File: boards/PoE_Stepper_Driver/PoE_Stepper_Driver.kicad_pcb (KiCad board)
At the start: 2 copper layers, 97.8 x 71.1 mm, 135 parts, among them J1 RJ45, J2 Motor, J3 Limits, J4 JTAG, J5 48V In, J6 12V, 3V3 Out, J7 PHY Data, J8 SPI Data, J9 UART, Q1 NMOS_POE, Q10 NMOS_POE, Q3 NMOS_POE, Q4 NMOS_POE, Q5 NMOS_POE, Q6 NMOS_POE, Q7 NMOS_POE, Q8 NMOS_POE, Q9 NMOS_POE, SW3 SW_Push, U1 LT4321, U14 DP83848C, U15 TMC429-I, U16 TMC2660C-PA, U2 LT4293, U3 STM32F407VETx, X1 SXO53C, Y1 8MHz

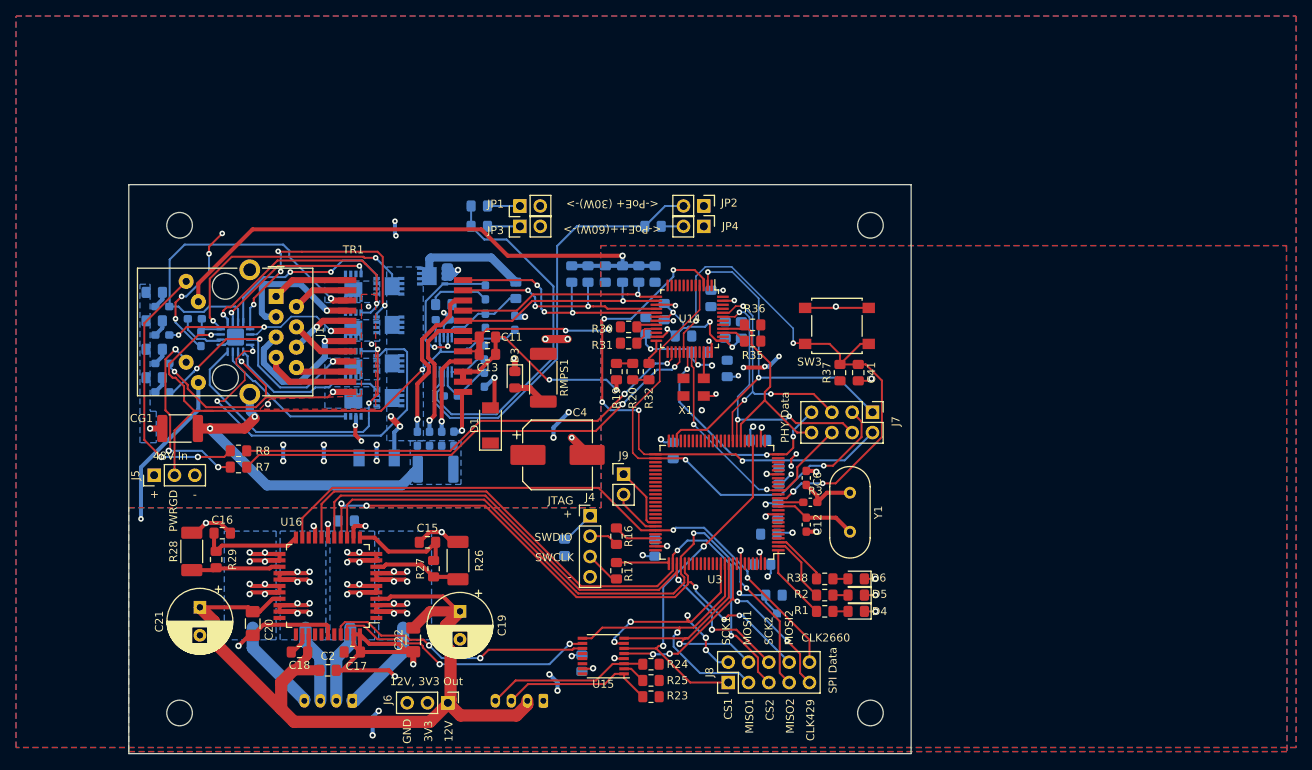
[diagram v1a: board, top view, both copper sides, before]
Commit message: made rev2 board changes
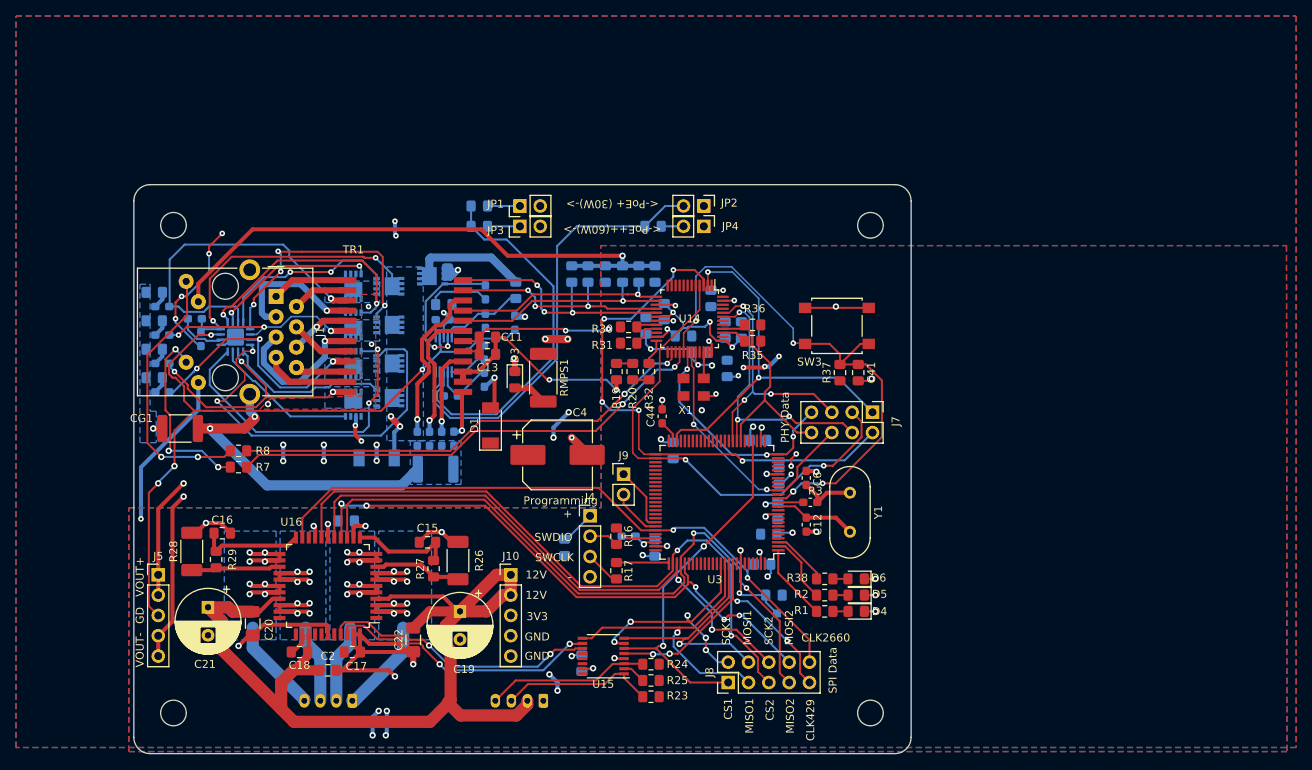
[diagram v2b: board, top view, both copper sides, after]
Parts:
- removed J6: 12V, 3V3 Out, Connector_PinHeader_2.54mm:PinHeader_1x03_P2.54mm_Vertical
- added C43: 2.2uF, Capacitor_SMD:C_0603_1608Metric_Pad1.05x0.95mm_HandSolder, B.Cu at (156.2, 101.7)
- added C44: 2.2uF, Capacitor_SMD:C_0603_1608Metric_Pad1.05x0.95mm_HandSolder, F.Cu at (160.4, 86.7)
- added J10: Converter Output, Connector_PinHeader_2.54mm:PinHeader_1x05_P2.54mm_Vertical, F.Cu at (141.5, 106.6)
- J4: value JTAG -> Programming
- J5: value 48V In -> Converter Input; footprint Connector_PinHeader_2.54mm:PinHeader_1x03_P2.54mm_Vertical -> Connector_PinHeader_2.54mm:PinHeader_1x05_P2.54mm_Vertical
- moved J5 12.5 mm to (97.4, 106.6), turned to 0 degrees
- moved C21 1.02 mm to (103.6, 110.6)
- moved REF** 0.76 mm to (99.3, 123.8)
- moved REF** 0.76 mm to (99.3, 62.9)
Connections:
- net SPI2_CS renamed SPI3_CS
- net SPI2_MISO renamed SPI3_MISO
- net SPI2_MOSI renamed SPI3_MOSI
- net SPI2_SCK renamed SPI3_SCK
- J5 pad 2: PWRGD -> VOUT+
- J5 pad 3: VOUT- -> PWRGD
- U3 pad 21: Net-(U3-Pad21) -> +3V3
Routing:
- net VOUT-: track 31.6 -> 52.9 mm, vias 13 -> 14
- net PWRGD: track 71.6 -> 91.0 mm, vias 2 -> 4
- net +12V: track 107.4 -> 123.9 mm
- net VOUT+: track 22.8 -> 38.1 mm, vias 13 -> 14
- net (no net): track 0.00 -> 3.10 mm, vias 0 -> 2
- net Net-(C43-Pad1): track 0.00 -> 3.00 mm, vias 0 -> 1
- net Net-(C44-Pad1): track 0.00 -> 2.76 mm
- net GND: track 127.3 -> 128.5 mm, vias 30 -> 31
- net /Motor_Control/DIR: track 34.0 -> 34.9 mm
- net /Motor_Control/STEP: track 33.6 -> 34.2 mm
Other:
- board size 97.8 x 71.1 mm -> 97.2 x 71.1 mm

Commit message: writing to 429 is working
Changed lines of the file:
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@@
       (drillshape 0)
       (scaleselection 1)
-      (outputdirectory "C:/Users/Bryan/Documents/Senior Design/PoE-Stepper-Motor-Driver/boards/gerbers/"))
+      (outputdirectory "C:/Users/Bryan/Documents/Senior Design/PoE-Stepper-Motor-Driver/boards/gerbers_main_rev2/"))
   )
   (net 0 "")
@@
       (effects (font (size 1 1) (thickness 0.15)))
     )
-    (pad 2 smd roundrect (at 2.225 0) (size 1.3 3.4) (layers F.Cu F.Paste F.Mask) (roundrect_rratio 0.1923076923076923)
+    (pad 2 smd roundrect (at 2.225 0) (size 1.3 3.4) (layers F.Cu F.Paste F.Mask) (roundrect_rratio 0.1923069230769231)
       (net 7 GNDPWR))
-    (pad 1 smd roundrect (at -2.225 0) (size 1.3 3.4) (layers F.Cu F.Paste F.Mask) (roundrect_rratio 0.1923076923076923)
+    (pad 1 smd roundrect (at -2.225 0) (size 1.3 3.4) (layers F.Cu F.Paste F.Mask) (roundrect_rratio 0.1923069230769231)
       (net 8 "Net-(CG1-Pad1)"))
     (model ${KISYS3DMOD}/Capacitor_SMD.3dshapes/C_1812_4532Metric.wrl
@@
       (effects (font (size 1 1) (thickness 0.15)) (justify mirror))
     )
-    (pad 1 smd roundrect (at -2.225 0 180) (size 1.3 3.4) (layers B.Cu B.Paste B.Mask) (roundrect_rratio 0.1923076923076923)
+    (pad 1 smd roundrect (at -2.225 0 180) (size 1.3 3.4) (layers B.Cu B.Paste B.Mask) (roundrect_rratio 0.1923069230769231)
       (net 9 "Net-(CG2-Pad1)"))
-    (pad 2 smd roundrect (at 2.225 0 180) (size 1.3 3.4) (layers B.Cu B.Paste B.Mask) (roundrect_rratio 0.1923076923076923)
+    (pad 2 smd roundrect (at 2.225 0 180) (size 1.3 3.4) (layers B.Cu B.Paste B.Mask) (roundrect_rratio 0.1923069230769231)
       (net 7 GNDPWR))
     (model ${KISYS3DMOD}/Capacitor_SMD.3dshapes/C_1812_4532Metric.wrl
